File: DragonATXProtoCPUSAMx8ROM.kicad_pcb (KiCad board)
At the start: 2 copper layers, 153.1 x 74.7 mm, 22 parts, among them IC1 HD63C09, IC11 74LS08, IC25 74LS244, IC3 74LS138, IC39 6883, IC4 74LS02, U4 28C256

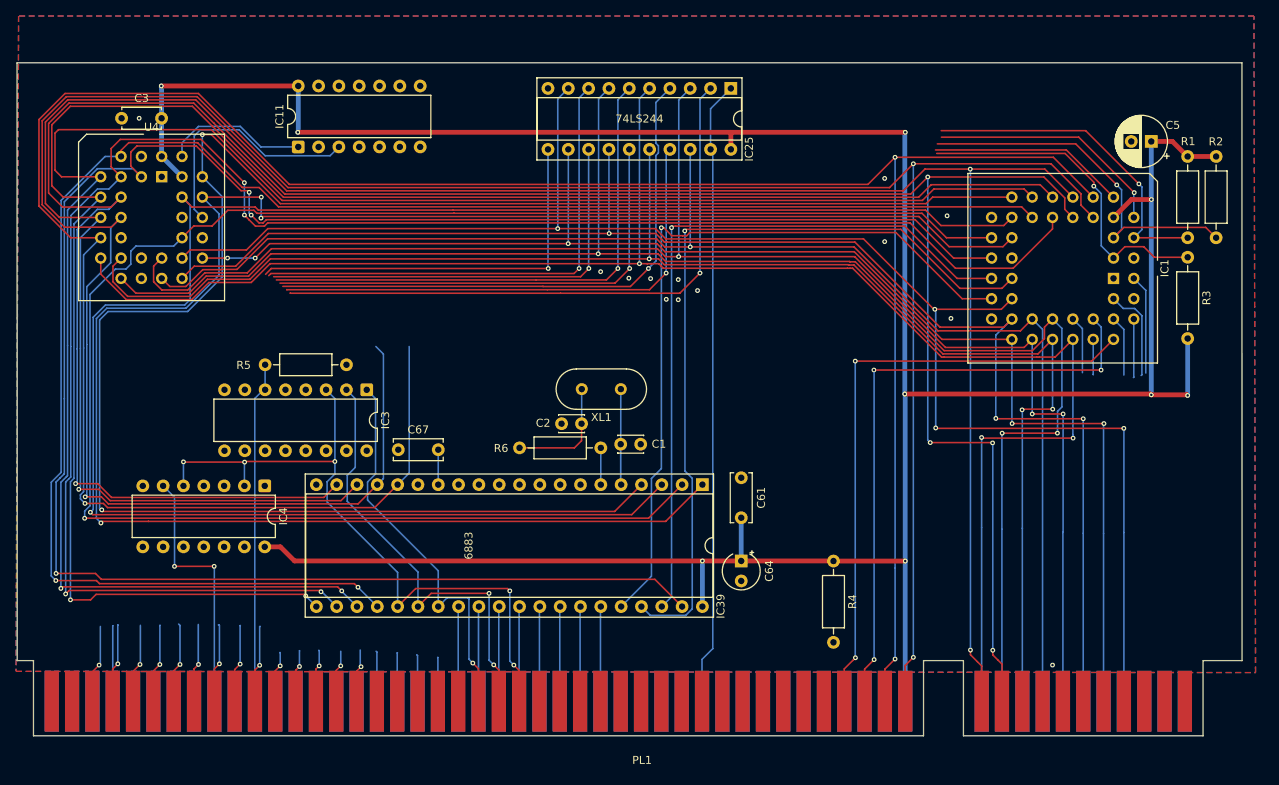
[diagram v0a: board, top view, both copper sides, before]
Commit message: wire in upper address lines for cartridge port
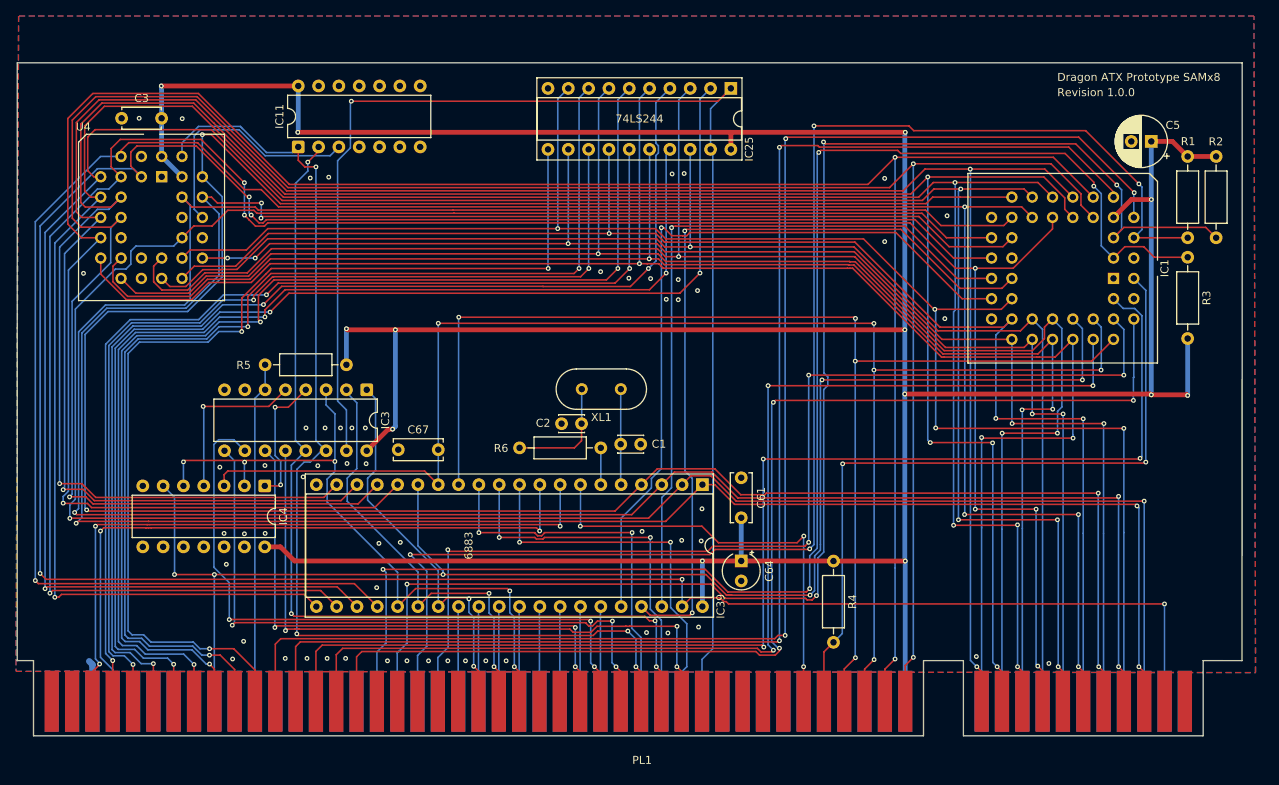
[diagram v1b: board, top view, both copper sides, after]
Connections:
- PL1 pad b33: unconnected-(PL1A-Pin_b33-Padb33) -> /D.OUT
- PL1 pad c3: unconnected-(PL1B-Pin_c3-Padc3) -> /A4
- PL1 pad c4: unconnected-(PL1B-Pin_c4-Padc4) -> /A5
- PL1 pad c5: unconnected-(PL1B-Pin_c5-Padc5) -> /A6
- PL1 pad c6: unconnected-(PL1B-Pin_c6-Padc6) -> /A7
- PL1 pad c7: unconnected-(PL1B-Pin_c7-Padc7) -> /A8
- PL1 pad c8: unconnected-(PL1B-Pin_c8-Padc8) -> /A9
- PL1 pad c9: unconnected-(PL1B-Pin_c9-Padc9) -> /A11
- PL1 pad d10: unconnected-(PL1B-Pin_d10-Padd10) -> /A12
- PL1 pad d9: unconnected-(PL1B-Pin_d9-Padd9) -> /A10
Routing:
- net /R/W: track 39.8 -> 188.7 mm, vias 2 -> 6
- net /BS: track 36.5 -> 183.1 mm, vias 2 -> 3
- net /BA: track 31.2 -> 174.2 mm, vias 1 -> 2
- net /TSC: track 18.5 -> 155.7 mm, vias 1 -> 3
- net /NMI: track 48.3 -> 183.9 mm, vias 1 -> 4
- net /IRQ: track 47.4 -> 180.6 mm, vias 1 -> 4
- net /FIRQ: track 51.8 -> 184.9 mm, vias 1 -> 4
- net /AVMA: track 14.0 -> 146.1 mm, vias 1 -> 3
- net /BUSY: track 10.9 -> 140.8 mm, vias 1 -> 3
- net /RST: track 13.0 -> 133.0 mm, vias 0 -> 4
- net /R0: track 18.1 -> 135.3 mm, vias 0 -> 4
- net /R1: track 0.00 -> 117.0 mm, vias 0 -> 4
- net /E: track 81.5 -> 186.6 mm, vias 3 -> 5
- net /D.OUT: track 78.3 -> 171.3 mm, vias 0 -> 1
- net +5V: track 365.2 -> 456.5 mm, vias 9 -> 13
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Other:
- outline, holes or cut-outs redrawn
- board text added: "Dragon ATX Prototype SAMx8"
- board text added: "Revision 1.0.0"
